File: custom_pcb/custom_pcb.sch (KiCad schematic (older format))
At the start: 290 parts, among them J1 USB_mini_micro_B, K0 KEYSW, K1 KEYSW, K10 KEYSW, K11 KEYSW, K12 KEYSW, K13 KEYSW, K14 KEYSW, K15 KEYSW, K16 KEYSW, K17 KEYSW, K18 KEYSW, K19 KEYSW, K2 KEYSW, K20 KEYSW, K21 KEYSW, K22 KEYSW, K23 KEYSW, K24 KEYSW, K25 KEYSW, K26 KEYSW, K27 KEYSW, K28 KEYSW, K29 KEYSW, K3 KEYSW, K30 KEYSW, K31 KEYSW, K32 KEYSW, K33 KEYSW, K34 KEYSW, K35 KEYSW, K36 KEYSW, K37 KEYSW, K38 KEYSW, K39 KEYSW, K4 KEYSW, K40 KEYSW, K41 KEYSW, K42 KEYSW, K43 KEYSW, K44 KEYSW, K45 KEYSW, K46 KEYSW, K47 KEYSW, K48 KEYSW, K49 KEYSW, K5 KEYSW, K50 KEYSW, K51 KEYSW, K52 KEYSW, K53 KEYSW, K54 KEYSW, K55 KEYSW, K56 KEYSW, K57 KEYSW, K58 KEYSW, K59 KEYSW, K6 KEYSW, K63 KEYSW, K64 KEYSW, K65 KEYSW, K66 KEYSW, K67 KEYSW, K68 KEYSW, K69 KEYSW, K7 KEYSW, K70 KEYSW, K71 KEYSW, K72 KEYSW, K73 KEYSW, K74 KEYSW, K75 KEYSW, K76 KEYSW, K77 KEYSW, K78 KEYSW, K79 KEYSW, K8 KEYSW, K80 KEYSW, K81 KEYSW, K82 KEYSW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

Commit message: cpcb hints to improve autorouting
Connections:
- wire segments 2491 -> 4110

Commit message: cpcb sane pin orderings
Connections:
- wire segments 4110 -> 2490
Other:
- moved on the sheet: R11, R12, R8, R9

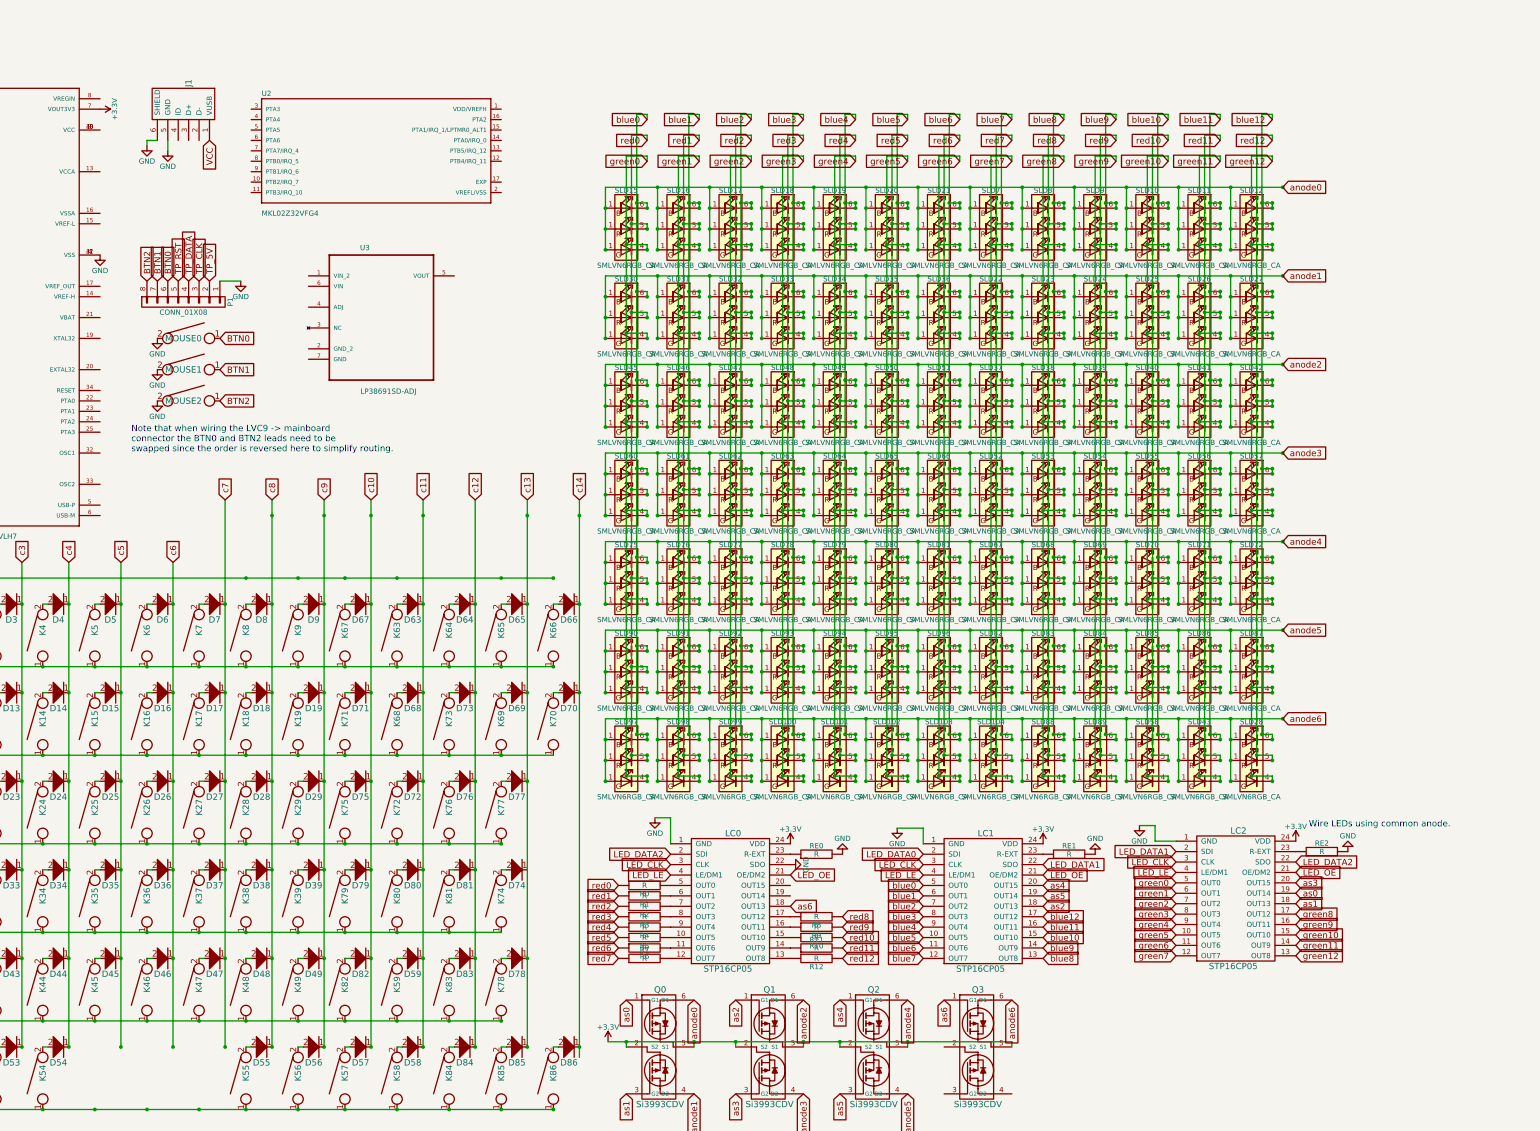
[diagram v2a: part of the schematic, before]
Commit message: added other teensy 3.2 parts, left out a bunch of the analog stuff
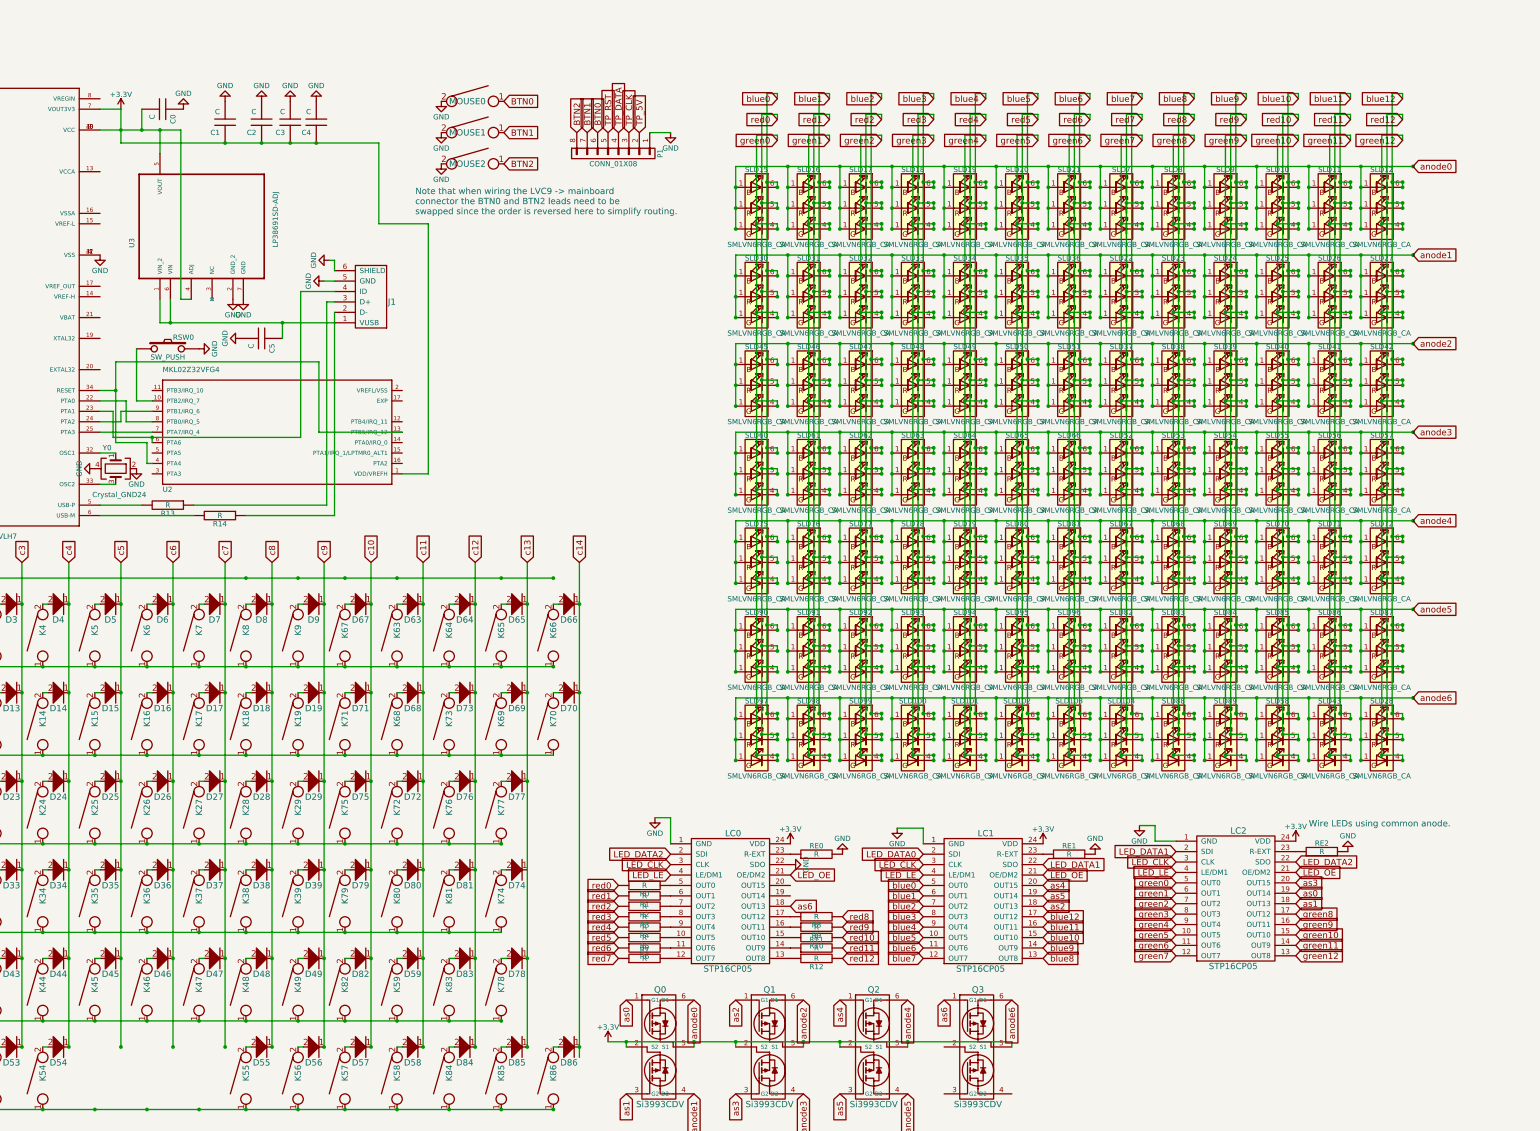
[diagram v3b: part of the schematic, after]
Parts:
- added C0, C1, C2, C3, C4, C5: C, Capacitors_SMD:C_0603_HandSoldering, symbol C
- added R13, R14: R, Resistors_SMD:R_0402_NoSilk, symbol R
- added RSW0: SW_PUSH, Buttons_Switches_SMD:SW_SPST_B3U-1000P, symbol SW_PUSH
- added Y0: Crystal_GND24, Crystals:Crystal_SMD_3225-4pin_3.2x2.5mm_HandSoldering, symbol Crystal_GND24
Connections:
- net labels removed: VCC
- wire segments 2490 -> 2538
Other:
- moved on the sheet: J1, MOUSE0, MOUSE1, MOUSE2, P1, SLD10, SLD100, SLD101, SLD102, SLD103, SLD104, SLD11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

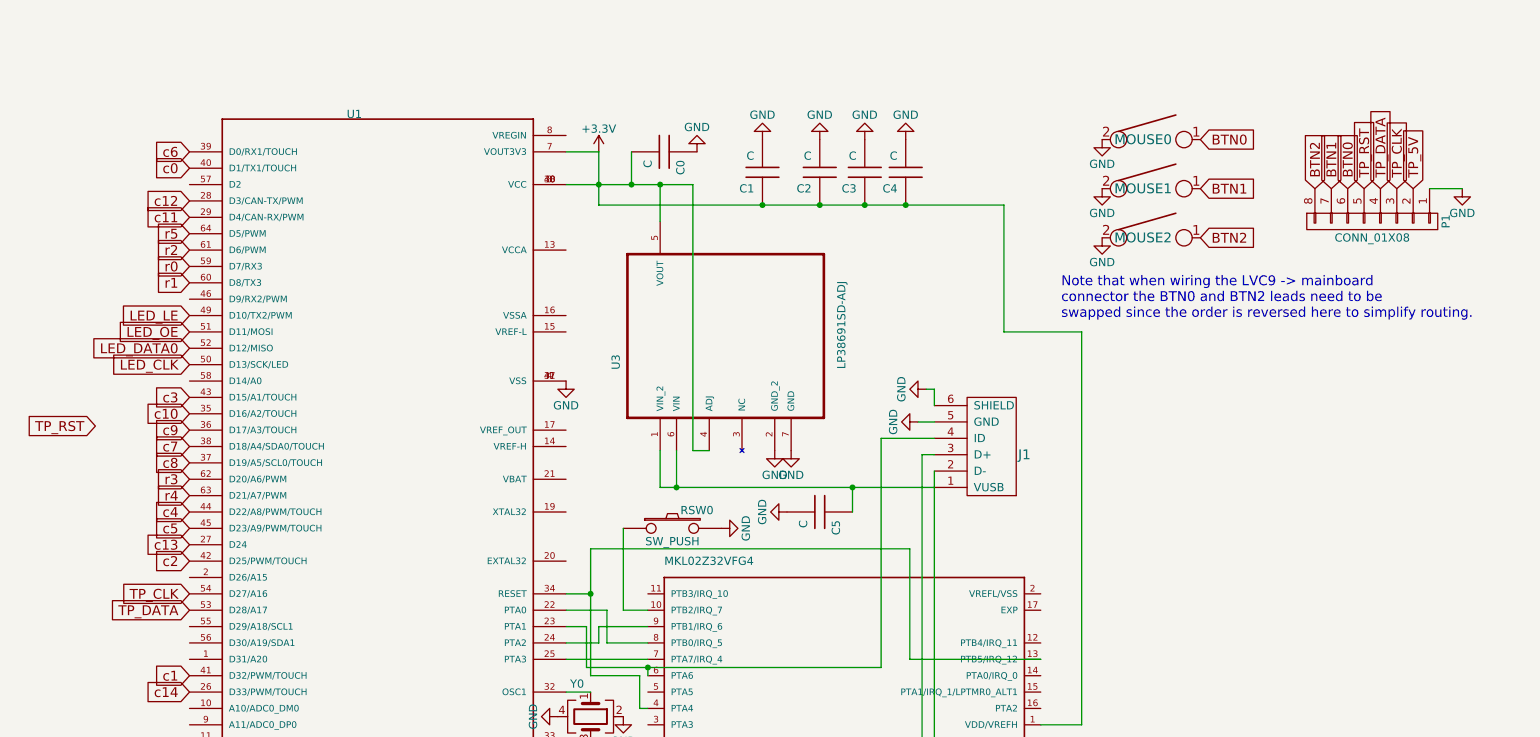
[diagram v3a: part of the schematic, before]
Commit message: cpcb timepoint before major led routing rework
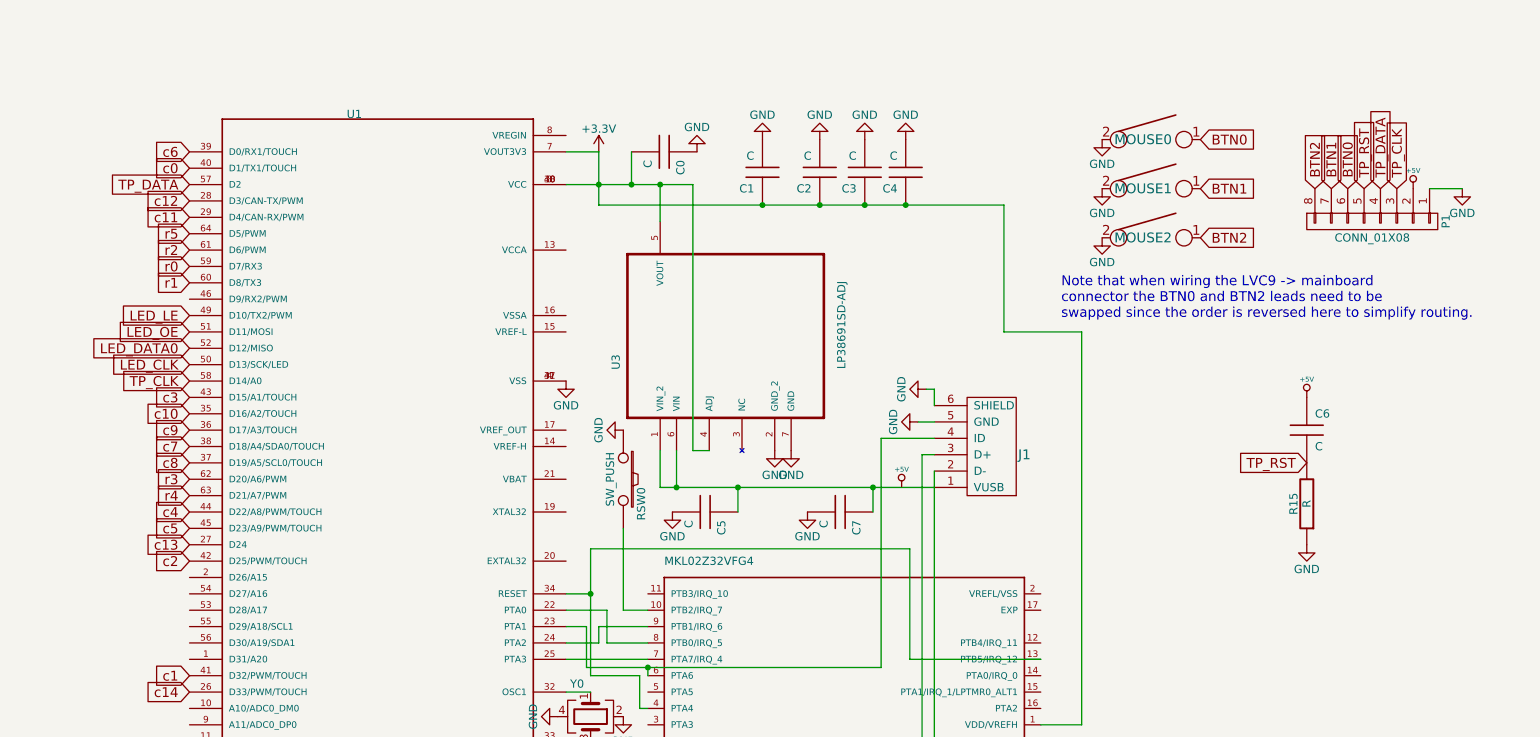
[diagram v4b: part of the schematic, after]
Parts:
- added C6, C7: C, Capacitors_SMD:C_0603_HandSoldering, symbol C
- added R15: R, Resistors_SMD:R_0402_NoSilk, symbol R
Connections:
- net labels added: +5V
- net labels removed: TP_5V
- wire segments 2538 -> 2539
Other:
- moved on the sheet: C5, RSW0
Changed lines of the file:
@@
 Text GLabel 1050 2050 0    60   Input ~ 0
 LED_DATA0
-Text GLabel 1050 3650 0    60   Input ~ 0
+Text GLabel 1050 1050 0    60   Input ~ 0
 TP_DATA
-Text GLabel 1050 3550 0    60   Input ~ 0
+Text GLabel 1050 2250 0    60   Input ~ 0
 TP_CLK
 Text GLabel 8325 1075 1    60   Input ~ 0
@@
 Text GLabel 8225 1075 1    60   Input ~ 0
 TP_RST
-Text GLabel 8525 1075 1    60   Input ~ 0
-TP_5V
 Text GLabel 7925 1075 1    60   Input ~ 0
 BTN2
@@
 Text GLabel 8325 8300 0    60   Input ~ 0
 red0
-Text GLabel 475  2525 0    60   Input ~ 0
+Text GLabel 7875 2750 0    60   Input ~ 0
 TP_RST
 $Comp
@@
 L C C5
 U 1 1 58DF3195
-P 4900 3050
-F 0 "C5" H 4950 3150 50  0000 L CNN
-F 1 "C" H 4950 2950 50  0000 L CNN
-F 2 "Capacitors_SMD:C_0603_HandSoldering" H 4900 3050 60  0001 C CNN
-F 3 "" H 4900 3050 60  0000 C CNN
-	1    4900 3050
+P 4200 3050
+F 0 "C5" H 4250 3150 50  0000 L CNN
+F 1 "C" H 4250 2950 50  0000 L CNN
+F 2 "Capacitors_SMD:C_0603_HandSoldering" H 4200 3050 60  0001 C CNN
+F 3 "" H 4200 3050 60  0000 C CNN
+	1    4200 3050
 	0    1    1    0
 $EndComp
@@
 L GND #PWR023
 U 1 1 58DF3B0D
-P 4700 3050
-F 0 "#PWR023" H 4700 2800 50  0001 C CNN
-F 1 "GND" H 4700 2900 50  0000 C CNN
-F 2 "" H 4700 3050 50  0000 C CNN
-F 3 "" H 4700 3050 50  0000 C CNN
-	1    4700 3050
-	0    1    -1   0
+P 4000 3050
+F 0 "#PWR023" H 4000 2800 50  0001 C CNN
+F 1 "GND" H 4000 2900 50  0000 C CNN
+F 2 "" H 4000 3050 50  0000 C CNN
+F 3 "" H 4000 3050 50  0000 C CNN
+	1    4000 3050
+	-1   0    0    -1
 $EndComp
 $Comp
 L SW_PUSH RSW0
 U 1 1 58E1198A
-P 4000 3150
-F 0 "RSW0" H 4150 3260 50  0000 C CNN
-F 1 "SW_PUSH" H 4000 3070 50  0000 C CNN
-F 2 "Buttons_Switches_SMD:SW_SPST_B3U-1000P" H 4000 3150 60  0001 C CNN
-F 3 "" H 4000 3150 60  0000 C CNN
-	1    4000 3150
-	1    0    0    -1
+P 3700 2850
+F 0 "RSW0" H 3850 2960 50  0000 C CNN
+F 1 "SW_PUSH" H 3700 2770 50  0000 C CNN
+F 2 "Buttons_Switches_SMD:SW_SPST_B3U-1000P" H 3700 2850 60  0001 C CNN
+F 3 "" H 3700 2850 60  0000 C CNN
+	1    3700 2850
+	0    1    1    0
 $EndComp
 $Comp
 L GND #PWR024
 U 1 1 58E11D54
-P 4300 3150
-F 0 "#PWR024" H 4300 2900 50  0001 C CNN
-F 1 "GND" H 4300 3000 50  0000 C CNN
-F 2 "" H 4300 3150 50  0000 C CNN
-F 3 "" H 4300 3150 50  0000 C CNN
-	1    4300 3150
-	0    -1   -1   0
+P 3700 2550
+F 0 "#PWR024" H 3700 2300 50  0001 C CNN
+F 1 "GND" H 3700 2400 50  0000 C CNN
+F 2 "" H 3700 2550 50  0000 C CNN
+F 3 "" H 3700 2550 50  0000 C CNN
+	1    3700 2550
+	0    1    1    0
 $EndComp
 $Comp
@@
 Connection ~ 4025 2900
 Wire Wire Line
-	5100 3050 5100 2900
-Connection ~ 5100 2900
-Wire Wire Line
 	3850 4050 3850 4000
 Wire Wire Line
@@
 Connection ~ 5175 1175
 Connection ~ 5425 1175
+$Comp
+L GND #PWR031
+U 1 1 58E939D5
+P 7875 3250
+F 0 "#PWR031" H 7875 3000 50  0001 C CNN
+F 1 "GND" H 7875 3100 50  0000 C CNN
+F 2 "" H 7875 3250 50  0000 C CNN
+F 3 "" H 7875 3250 50  0000 C CNN
+	1    7875 3250
+	1    0    0    -1
+$EndComp
+$Comp
+L C C6
+U 1 1 58E93D64
+P 7875 2550
+F 0 "C6" H 7925 2650 50  0000 L CNN
+F 1 "C" H 7925 2450 50  0000 L CNN
+F 2 "Capacitors_SMD:C_0603_HandSoldering" H 7875 2550 60  0001 C CNN
+F 3 "" H 7875 2550 60  0000 C CNN
+	1    7875 2550
+	1    0    0    -1
+$EndComp
+$Comp
+L R R15
+U 1 1 58E94E7C
+P 7875 3000
+F 0 "R15" V 7955 3000 50  0000 C CNN
+F 1 "R" V 7875 3000 50  0000 C CNN
+F 2 "Resistors_SMD:R_0402_NoSilk" H 7875 3000 60  0001 C CNN
+F 3 "" H 7875 3000 60  0000 C CNN
+	1    7875 3000
+	-1   0    0    1
+$EndComp
+$Comp
+L +5V #PWR032
+U 1 1 58E9843E
+P 7875 2350
+F 0 "#PWR032" H 7875 2320 20  0001 C CNN
+F 1 "+5V" H 7875 2460 30  0000 C CNN
+F 2 "" H 7875 2350 60  0000 C CNN
+F 3 "" H 7875 2350 60  0000 C CNN
+	1    7875 2350
+	1    0    0    -1
+$EndComp
+$Comp
+L +5V #PWR033
+U 1 1 58EA0A47
+P 5400 2900
+F 0 "#PWR033" H 5400 2870 20  0001 C CNN
+F 1 "+5V" H 5400 3010 30  0000 C CNN
+F 2 "" H 5400 2900 60  0000 C CNN
+F 3 "" H 5400 2900 60  0000 C CNN
+	1    5400 2900
+	1    0    0    -1
+$EndComp
+$Comp
+L C C7
+U 1 1 58EA3DC4
+P 5025 3050
+F 0 "C7" H 5075 3150 50  0000 L CNN
+F 1 "C" H 5075 2950 50  0000 L CNN
+F 2 "Capacitors_SMD:C_0603_HandSoldering" H 5025 3050 60  0001 C CNN
+F 3 "" H 5025 3050 60  0000 C CNN
+	1    5025 3050
+	0    1    1    0
+$EndComp
+$Comp
+L GND #PWR034
+U 1 1 58EA4EC0
+P 4825 3050
+F 0 "#PWR034" H 4825 2800 50  0001 C CNN
+F 1 "GND" H 4825 2900 50  0000 C CNN
+F 2 "" H 4825 3050 50  0000 C CNN
+F 3 "" H 4825 3050 50  0000 C CNN
+	1    4825 3050
+	-1   0    0    -1
+$EndComp
+Wire Wire Line
+	5225 3050 5225 2900
+Connection ~ 5225 2900
+Wire Wire Line
+	4400 3050 4400 2900
+Connection ~ 4400 2900
+$Comp
+L +5V #PWR035
+U 1 1 58EAFE75
+P 8525 1075
+F 0 "#PWR035" H 8525 1045 20  0001 C CNN
+F 1 "+5V" H 8525 1185 30  0000 C CNN
+F 2 "" H 8525 1075 60  0000 C CNN
+F 3 "" H 8525 1075 60  0000 C CNN
+	1    8525 1075
+	1    0    0    -1
+$EndComp
 $EndSCHEMATC

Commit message: routing of the tricky bits and discovered and added the MKL04Z32
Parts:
- U2: value MKL02Z32VFG4 -> MKL04Z32; footprint MKL02Z32VFG4:QFN50P300X300X65-17N -> cherry_rgb:QFP50P900X900X160-48N; symbol MKL02Z32VFG4 -> MKL04Z32; Availability Good -> (none); Package QFN-16 NXP Semiconductors -> (none); Price 1.33 USD -> (none)
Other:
- moved on the sheet: LC0, LC1, LC2, R0, R1, R10, R11, R12, R2, R3, R4, R5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

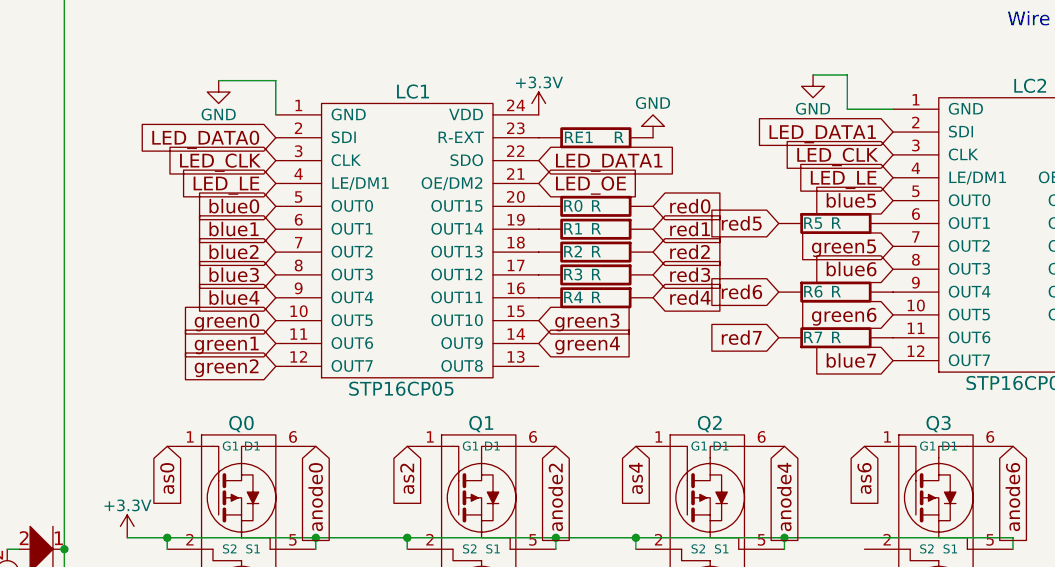
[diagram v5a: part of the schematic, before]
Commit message: cpcb more sane pin ordering
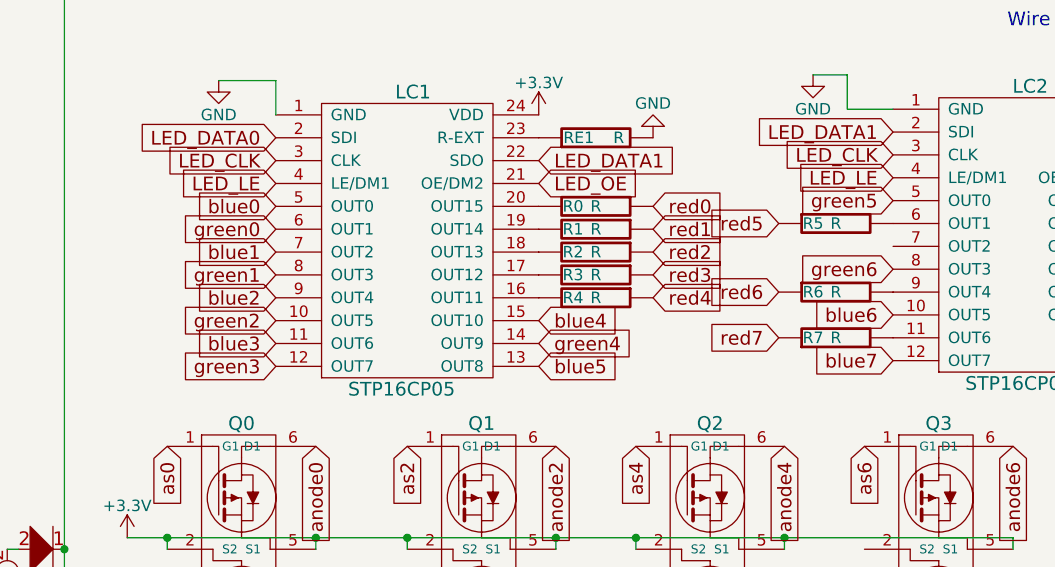
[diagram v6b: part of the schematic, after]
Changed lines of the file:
@@
 Text GLabel 8875 8350 0    60   Input ~ 0
 blue0
+Text GLabel 8875 8450 0    60   Input ~ 0
+green0
+Text GLabel 8875 8550 0    60   Input ~ 0
+blue1
+Text GLabel 8875 8650 0    60   Input ~ 0
+green1
+Text GLabel 8875 8750 0    60   Input ~ 0
+blue2
 Text GLabel 8875 8850 0    60   Input ~ 0
-green0
-Text GLabel 8875 8450 0    60   Input ~ 0
-blue1
+green2
 Text GLabel 8875 8950 0    60   Input ~ 0
-green1
-Text GLabel 8875 8550 0    60   Input ~ 0
-blue2
+blue3
 Text GLabel 8875 9050 0    60   Input ~ 0
-green2
-Text GLabel 8875 8650 0    60   Input ~ 0
-blue3
+green3
 Text GLabel 10025 8850 2    60   Input ~ 0
-green3
-Text GLabel 8875 8750 0    60   Input ~ 0
 blue4
 Text GLabel 10025 8950 2    60   Input ~ 0
 green4
+Text GLabel 10025 9050 2    60   Input ~ 0
+blue5
 Text GLabel 11575 8325 0    60   Input ~ 0
-blue5
-Text GLabel 11575 8525 0    60   Input ~ 0
 green5
-Text GLabel 11575 8625 0    60   Input ~ 0
+Text GLabel 11575 8825 0    60   Input ~ 0
 blue6
 Text GLabel 11075 8725 0    60   Input ~ 0
 red6
-Text GLabel 11575 8825 0    60   Input ~ 0
+Text GLabel 11575 8625 0    60   Input ~ 0
 green6
 Text GLabel 11075 8425 0    60   Input ~ 0
